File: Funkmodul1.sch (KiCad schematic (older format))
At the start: 48 parts, among them Q1 SSM3J334RLFTR-ND, Q2 AO3414, U1 MC74HC4538A, U2 MAX892, U3 ATMEGA128-16AU, Y1 Crystal_GND24

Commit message: Places µC of second module
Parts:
- Q1: symbol Q_PMOS_DGS -> Q_PMOS_SGD
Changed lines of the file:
@@
 $EndComp
 $Comp
-L GND #PWR11
+L GND #PWR01
 U 1 1 59FF9D54
 P 3200 1650
-F 0 "#PWR11" H 3200 1400 50  0001 C CNN
+F 0 "#PWR01" H 3200 1400 50  0001 C CNN
 F 1 "GND" H 3200 1500 50  0000 C CNN
 F 2 "" H 3200 1650 50  0001 C CNN
@@
 $EndComp
 $Comp
-L GND #PWR7
+L GND #PWR02
 U 1 1 59B7E738
 P 2250 1350
-F 0 "#PWR7" H 2250 1100 50  0001 C CNN
+F 0 "#PWR02" H 2250 1100 50  0001 C CNN
 F 1 "GND" H 2250 1200 50  0000 C CNN
 F 2 "" H 2250 1350 50  0001 C CNN
@@
 VCC
 $Comp
-L GND #PWR13
+L GND #PWR03
 U 1 1 59B80D24
 P 3750 2450
-F 0 "#PWR13" H 3750 2200 50  0001 C CNN
+F 0 "#PWR03" H 3750 2200 50  0001 C CNN
 F 1 "GND" H 3750 2300 50  0000 C CNN
 F 2 "" H 3750 2450 50  0001 C CNN
@@
 $EndComp
 $Comp
-L GND #PWR14
+L GND #PWR04
 U 1 1 59B80D8A
 P 3750 2850
-F 0 "#PWR14" H 3750 2600 50  0001 C CNN
+F 0 "#PWR04" H 3750 2600 50  0001 C CNN
 F 1 "GND" H 3750 2700 50  0000 C CNN
 F 2 "" H 3750 2850 50  0001 C CNN
@@
 $EndComp
 $Comp
-L GND #PWR17
+L GND #PWR05
 U 1 1 59B80E1B
 P 4300 3350
-F 0 "#PWR17" H 4300 3100 50  0001 C CNN
+F 0 "#PWR05" H 4300 3100 50  0001 C CNN
 F 1 "GND" H 4300 3200 50  0000 C CNN
 F 2 "" H 4300 3350 50  0001 C CNN
@@
 $EndComp
 $Comp
-L GND #PWR18
+L GND #PWR06
 U 1 1 59FF9D5A
 P 4550 2350
-F 0 "#PWR18" H 4550 2100 50  0001 C CNN
+F 0 "#PWR06" H 4550 2100 50  0001 C CNN
 F 1 "GND" H 4550 2200 50  0000 C CNN
 F 2 "" H 4550 2350 50  0001 C CNN
@@
 $EndComp
 $Comp
-L GND #PWR19
+L GND #PWR07
 U 1 1 59FF9D5B
 P 5000 2350
-F 0 "#PWR19" H 5000 2100 50  0001 C CNN
+F 0 "#PWR07" H 5000 2100 50  0001 C CNN
 F 1 "GND" H 5000 2200 50  0000 C CNN
 F 2 "" H 5000 2350 50  0001 C CNN
@@
 $EndComp
 $Comp
-L GND #PWR24
+L GND #PWR08
 U 1 1 59FF9D5C
 P 7000 1100
-F 0 "#PWR24" H 7000 850 50  0001 C CNN
+F 0 "#PWR08" H 7000 850 50  0001 C CNN
 F 1 "GND" H 7000 950 50  0000 C CNN
 F 2 "" H 7000 1100 50  0001 C CNN
@@
 $EndComp
 $Comp
-L GND #PWR21
+L GND #PWR09
 U 1 1 59FF9D5D
 P 6500 1150
-F 0 "#PWR21" H 6500 900 50  0001 C CNN
+F 0 "#PWR09" H 6500 900 50  0001 C CNN
 F 1 "GND" H 6500 1000 50  0000 C CNN
 F 2 "" H 6500 1150 50  0001 C CNN
@@
 $EndComp
 $Comp
-L GND #PWR20
+L GND #PWR010
 U 1 1 59FF9D5E
 P 6200 1150
-F 0 "#PWR20" H 6200 900 50  0001 C CNN
+F 0 "#PWR010" H 6200 900 50  0001 C CNN
 F 1 "GND" H 6200 1000 50  0000 C CNN
 F 2 "" H 6200 1150 50  0001 C CNN
@@
 $EndComp
 $Comp
-L GND #PWR22
+L GND #PWR011
 U 1 1 59B847A7
 P 6600 5700
-F 0 "#PWR22" H 6600 5450 50  0001 C CNN
+F 0 "#PWR011" H 6600 5450 50  0001 C CNN
 F 1 "GND" H 6600 5550 50  0000 C CNN
 F 2 "" H 6600 5700 50  0001 C CNN
@@
 $EndComp
 $Comp
-L GND #PWR23
+L GND #PWR012
 U 1 1 59B8480D
 P 6700 5700
-F 0 "#PWR23" H 6700 5450 50  0001 C CNN
+F 0 "#PWR012" H 6700 5450 50  0001 C CNN
 F 1 "GND" H 6700 5550 50  0000 C CNN
 F 2 "" H 6700 5700 50  0001 C CNN
@@
 $EndComp
 $Comp
-L GND #PWR25
+L GND #PWR013
 U 1 1 59B84873
 P 7000 5700
-F 0 "#PWR25" H 7000 5450 50  0001 C CNN
+F 0 "#PWR013" H 7000 5450 50  0001 C CNN
 F 1 "GND" H 7000 5550 50  0000 C CNN
 F 2 "" H 7000 5700 50  0001 C CNN
@@
 $EndComp
 $Comp
-L GND #PWR5
+L GND #PWR014
 U 1 1 59B8BFBA
 P 1650 2750
-F 0 "#PWR5" H 1650 2500 50  0001 C CNN
+F 0 "#PWR014" H 1650 2500 50  0001 C CNN
 F 1 "GND" H 1650 2600 50  0000 C CNN
 F 2 "" H 1650 2750 50  0001 C CNN
@@
 $EndComp
 $Comp
-L GND #PWR12
+L GND #PWR015
 U 1 1 59B8D4AD
 P 3600 750
-F 0 "#PWR12" H 3600 500 50  0001 C CNN
+F 0 "#PWR015" H 3600 500 50  0001 C CNN
 F 1 "GND" H 3600 600 50  0000 C CNN
 F 2 "" H 3600 750 50  0001 C CNN
@@
 $EndComp
 $Comp
-L GND #PWR6
+L GND #PWR016
 U 1 1 59FF9D6A
 P 1750 750
-F 0 "#PWR6" H 1750 500 50  0001 C CNN
+F 0 "#PWR016" H 1750 500 50  0001 C CNN
 F 1 "GND" H 1750 600 50  0000 C CNN
 F 2 "" H 1750 750 50  0001 C CNN
@@
 $EndComp
 $Comp
-L GND #PWR8
+L GND #PWR017
 U 1 1 59FF9D6F
 P 2650 4050
-F 0 "#PWR8" H 2650 3800 50  0001 C CNN
+F 0 "#PWR017" H 2650 3800 50  0001 C CNN
 F 1 "GND" H 2650 3900 50  0000 C CNN
 F 2 "" H 2650 4050 50  0001 C CNN
@@
 $EndComp
 $Comp
-L GND #PWR1
+L GND #PWR018
 U 1 1 59FF9D78
 P 600 1500
-F 0 "#PWR1" H 600 1250 50  0001 C CNN
+F 0 "#PWR018" H 600 1250 50  0001 C CNN
 F 1 "GND" H 600 1350 50  0000 C CNN
 F 2 "" H 600 1500 50  0001 C CNN
@@
 $EndComp
 $Comp
-L GND #PWR2
+L GND #PWR019
 U 1 1 59C31F10
 P 800 4850
-F 0 "#PWR2" H 800 4600 50  0001 C CNN
+F 0 "#PWR019" H 800 4600 50  0001 C CNN
 F 1 "GND" H 800 4700 50  0000 C CNN
 F 2 "" H 800 4850 50  0001 C CNN
@@
 $EndComp
 $Comp
-L GND #PWR10
+L GND #PWR020
 U 1 1 59C39B79
 P 2950 3100
-F 0 "#PWR10" H 2950 2850 50  0001 C CNN
+F 0 "#PWR020" H 2950 2850 50  0001 C CNN
 F 1 "GND" H 2950 2950 50  0000 C CNN
 F 2 "" H 2950 3100 50  0001 C CNN
@@
 $EndComp
 $Comp
-L GND #PWR3
+L GND #PWR021
 U 1 1 59C3C15C
 P 1350 3400
-F 0 "#PWR3" H 1350 3150 50  0001 C CNN
+F 0 "#PWR021" H 1350 3150 50  0001 C CNN
 F 1 "GND" H 1350 3250 50  0000 C CNN
 F 2 "" H 1350 3400 50  0001 C CNN
@@
 $EndComp
 $Comp
-L GND #PWR9
+L GND #PWR022
 U 1 1 59C3F3E3
 P 2700 5750
-F 0 "#PWR9" H 2700 5500 50  0001 C CNN
+F 0 "#PWR022" H 2700 5500 50  0001 C CNN
 F 1 "GND" H 2700 5600 50  0000 C CNN
 F 2 "" H 2700 5750 50  0001 C CNN
@@
 $EndComp
 $Comp
-L GND #PWR15
+L GND #PWR023
 U 1 1 59C3FC57
 P 3750 5550
-F 0 "#PWR15" H 3750 5300 50  0001 C CNN
+F 0 "#PWR023" H 3750 5300 50  0001 C CNN
 F 1 "GND" H 3750 5400 50  0000 C CNN
 F 2 "" H 3750 5550 50  0001 C CNN
@@
 $EndComp
 $Comp
-L GND #PWR16
+L GND #PWR024
 U 1 1 59C4457A
 P 3950 5500
-F 0 "#PWR16" H 3950 5250 50  0001 C CNN
+F 0 "#PWR024" H 3950 5250 50  0001 C CNN
 F 1 "GND" H 3950 5350 50  0000 C CNN
 F 2 "" H 3950 5500 50  0001 C CNN
@@
 VCC
 $Comp
-L GND #PWR26
+L GND #PWR025
 U 1 1 59D3B876
 P 9100 1450
-F 0 "#PWR26" H 9100 1200 50  0001 C CNN
+F 0 "#PWR025" H 9100 1200 50  0001 C CNN
 F 1 "GND" H 9100 1300 50  0000 C CNN
 F 2 "" H 9100 1450 50  0001 C CNN
@@
 $EndComp
 $Comp
-L GND #PWR4
+L GND #PWR026
 U 1 1 59FF9DAA
 P 1600 2400
-F 0 "#PWR4" H 1600 2150 50  0001 C CNN
+F 0 "#PWR026" H 1600 2150 50  0001 C CNN
 F 1 "GND" H 1600 2250 50  0000 C CNN
 F 2 "" H 1600 2400 50  0001 C CNN
@@
 3.3V
 $Comp
-L Q_PMOS_DGS Q1
+L Q_PMOS_SGD Q1
 U 1 1 59FF9DB0
 P 1400 1500

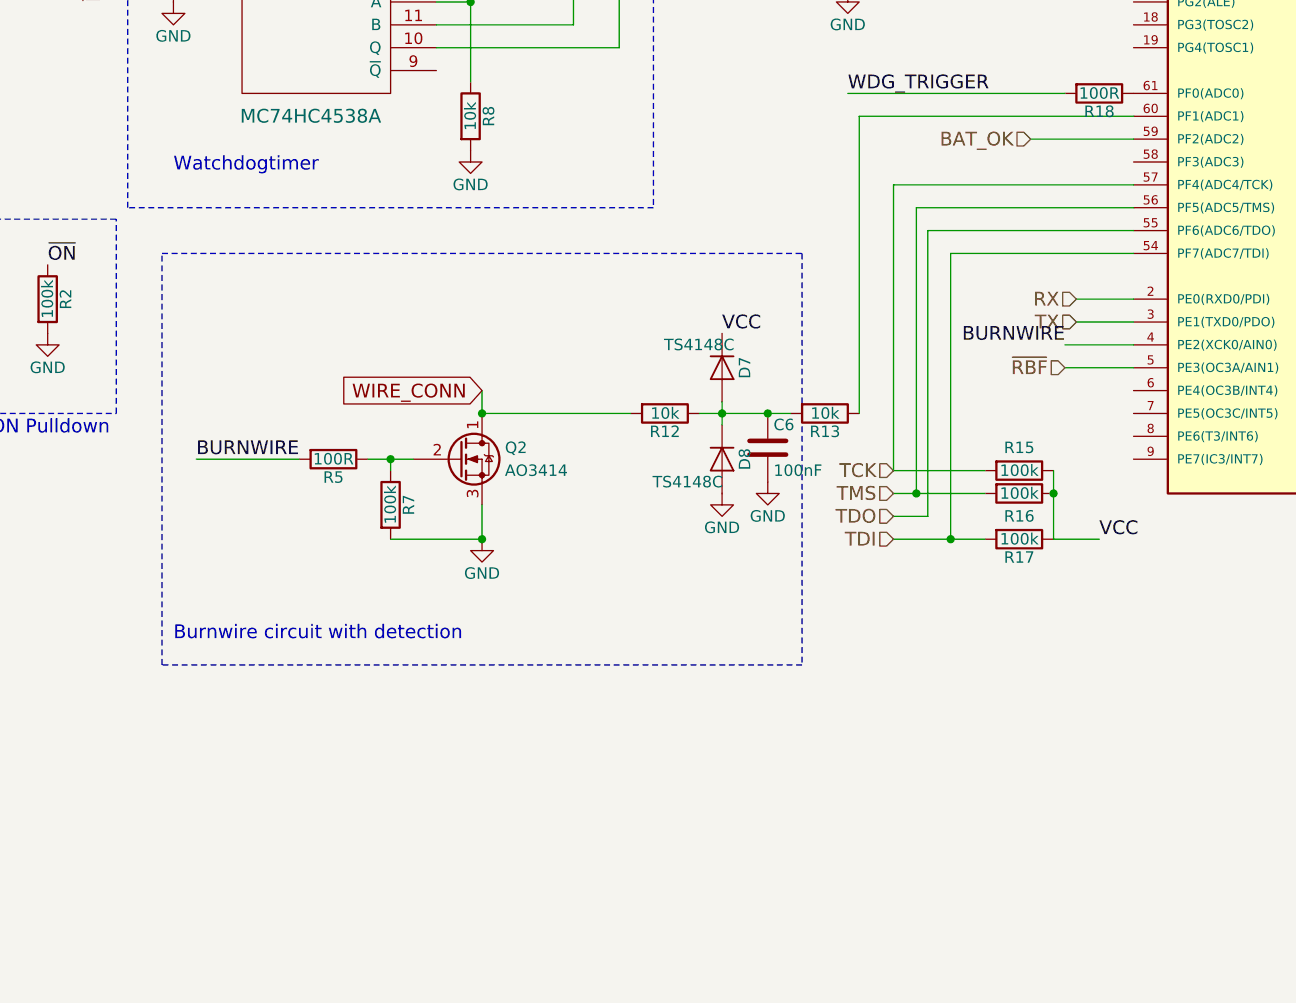
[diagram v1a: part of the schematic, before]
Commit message: Places all Components of second module
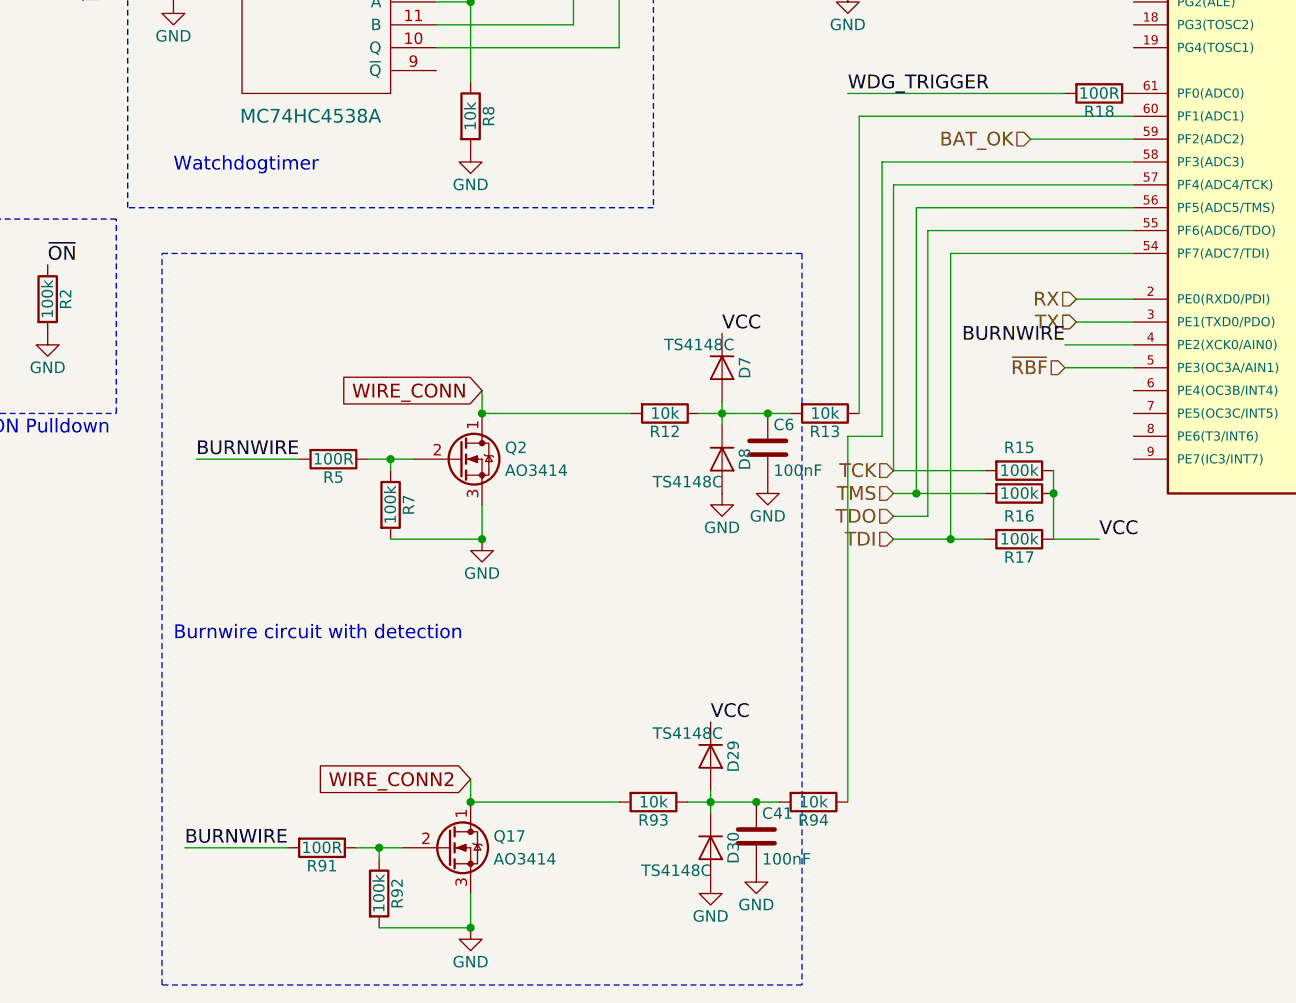
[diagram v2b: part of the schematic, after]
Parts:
- added C41: 100nF, Capacitors_SMD:C_0603_HandSoldering, symbol C
- added D29, D30: TS4148C, Diodes_SMD:D_0603, symbol D
- added Q17: AO3414, TO_SOT_Packages_SMD:SOT-23, symbol Q_NMOS_DGS
- added R91: 100R, Resistors_SMD:R_0603_HandSoldering, symbol R
- added R92: 100k, Resistors_SMD:R_0603_HandSoldering, symbol R
- added R93, R94: 10k, Resistors_SMD:R_0603_HandSoldering, symbol R
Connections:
- net BURNWIRE: now also R91.2
- net GND: now also C41.2, D30.2 (A), Q17.3 (S), R92.2
- net VCC: now also D29.1 (K)
- net at U3.58 (PF3(ADC3)): now also R94.1
- new net: Q17.2 (G), R91.1, R92.1
- new net: C41.1, D29.2 (A), D30.1 (K), R93.1, R94.2
- new net WIRE_CONN2: Q17.1 (D), R93.2

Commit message: Adds second burnwire fets
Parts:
- removed R15, R16, R17: 100k, Resistors_SMD:R_0603_HandSoldering, symbol R
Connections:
- net BURNWIRE: no longer R91.2
- net BURNWIRE2: now reaches U3.6 (PE4(OC3B/INT4))
- net BURNWIRE2: now also R91.2
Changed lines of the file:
@@
 $EndComp
 $Comp
-L GND #PWR12
+L GND #PWR01
 U 1 1 59FF9D54
 P 3200 1650
-F 0 "#PWR12" H 3200 1400 50  0001 C CNN
+F 0 "#PWR01" H 3200 1400 50  0001 C CNN
 F 1 "GND" H 3200 1500 50  0000 C CNN
 F 2 "" H 3200 1650 50  0001 C CNN
@@
 $EndComp
 $Comp
-L GND #PWR7
+L GND #PWR02
 U 1 1 59B7E738
 P 2250 1350
-F 0 "#PWR7" H 2250 1100 50  0001 C CNN
+F 0 "#PWR02" H 2250 1100 50  0001 C CNN
 F 1 "GND" H 2250 1200 50  0000 C CNN
 F 2 "" H 2250 1350 50  0001 C CNN
@@
 VCC
 $Comp
-L GND #PWR15
+L GND #PWR03
 U 1 1 59B80D24
 P 3750 2450
-F 0 "#PWR15" H 3750 2200 50  0001 C CNN
+F 0 "#PWR03" H 3750 2200 50  0001 C CNN
 F 1 "GND" H 3750 2300 50  0000 C CNN
 F 2 "" H 3750 2450 50  0001 C CNN
@@
 $EndComp
 $Comp
-L GND #PWR16
+L GND #PWR04
 U 1 1 59B80D8A
 P 3750 2850
-F 0 "#PWR16" H 3750 2600 50  0001 C CNN
+F 0 "#PWR04" H 3750 2600 50  0001 C CNN
 F 1 "GND" H 3750 2700 50  0000 C CNN
 F 2 "" H 3750 2850 50  0001 C CNN
@@
 $EndComp
 $Comp
-L GND #PWR20
+L GND #PWR05
 U 1 1 59B80E1B
 P 4300 3350
-F 0 "#PWR20" H 4300 3100 50  0001 C CNN
+F 0 "#PWR05" H 4300 3100 50  0001 C CNN
 F 1 "GND" H 4300 3200 50  0000 C CNN
 F 2 "" H 4300 3350 50  0001 C CNN
@@
 $EndComp
 $Comp
-L GND #PWR21
+L GND #PWR06
 U 1 1 59FF9D5A
 P 4550 2350
-F 0 "#PWR21" H 4550 2100 50  0001 C CNN
+F 0 "#PWR06" H 4550 2100 50  0001 C CNN
 F 1 "GND" H 4550 2200 50  0000 C CNN
 F 2 "" H 4550 2350 50  0001 C CNN
@@
 $EndComp
 $Comp
-L GND #PWR22
+L GND #PWR07
 U 1 1 59FF9D5B
 P 5000 2350
-F 0 "#PWR22" H 5000 2100 50  0001 C CNN
+F 0 "#PWR07" H 5000 2100 50  0001 C CNN
 F 1 "GND" H 5000 2200 50  0000 C CNN
 F 2 "" H 5000 2350 50  0001 C CNN
@@
 $EndComp
 $Comp
-L GND #PWR27
+L GND #PWR08
 U 1 1 59FF9D5C
 P 7000 1100
-F 0 "#PWR27" H 7000 850 50  0001 C CNN
+F 0 "#PWR08" H 7000 850 50  0001 C CNN
 F 1 "GND" H 7000 950 50  0000 C CNN
 F 2 "" H 7000 1100 50  0001 C CNN
@@
 $EndComp
 $Comp
-L GND #PWR24
+L GND #PWR09
 U 1 1 59FF9D5D
 P 6500 1150
-F 0 "#PWR24" H 6500 900 50  0001 C CNN
+F 0 "#PWR09" H 6500 900 50  0001 C CNN
 F 1 "GND" H 6500 1000 50  0000 C CNN
 F 2 "" H 6500 1150 50  0001 C CNN
@@
 $EndComp
 $Comp
-L GND #PWR23
+L GND #PWR010
 U 1 1 59FF9D5E
 P 6200 1150
-F 0 "#PWR23" H 6200 900 50  0001 C CNN
+F 0 "#PWR010" H 6200 900 50  0001 C CNN
 F 1 "GND" H 6200 1000 50  0000 C CNN
 F 2 "" H 6200 1150 50  0001 C CNN
@@
 $EndComp
 $Comp
-L GND #PWR25
+L GND #PWR011
 U 1 1 59B847A7
 P 6600 5700
-F 0 "#PWR25" H 6600 5450 50  0001 C CNN
+F 0 "#PWR011" H 6600 5450 50  0001 C CNN
 F 1 "GND" H 6600 5550 50  0000 C CNN
 F 2 "" H 6600 5700 50  0001 C CNN
@@
 $EndComp
 $Comp
-L GND #PWR26
+L GND #PWR012
 U 1 1 59B8480D
 P 6700 5700
-F 0 "#PWR26" H 6700 5450 50  0001 C CNN
+F 0 "#PWR012" H 6700 5450 50  0001 C CNN
 F 1 "GND" H 6700 5550 50  0000 C CNN
 F 2 "" H 6700 5700 50  0001 C CNN
@@
 $EndComp
 $Comp
-L GND #PWR28
+L GND #PWR013
 U 1 1 59B84873
 P 7000 5700
-F 0 "#PWR28" H 7000 5450 50  0001 C CNN
+F 0 "#PWR013" H 7000 5450 50  0001 C CNN
 F 1 "GND" H 7000 5550 50  0000 C CNN
 F 2 "" H 7000 5700 50  0001 C CNN
@@
 $EndComp
 $Comp
-L GND #PWR5
+L GND #PWR014
 U 1 1 59B8BFBA
 P 1650 2750
-F 0 "#PWR5" H 1650 2500 50  0001 C CNN
+F 0 "#PWR014" H 1650 2500 50  0001 C CNN
 F 1 "GND" H 1650 2600 50  0000 C CNN
 F 2 "" H 1650 2750 50  0001 C CNN
@@
 $EndComp
 $Comp
-L GND #PWR13
+L GND #PWR015
 U 1 1 59B8D4AD
 P 3600 750
-F 0 "#PWR13" H 3600 500 50  0001 C CNN
+F 0 "#PWR015" H 3600 500 50  0001 C CNN
 F 1 "GND" H 3600 600 50  0000 C CNN
 F 2 "" H 3600 750 50  0001 C CNN
@@
 $EndComp
 $Comp
-L GND #PWR6
+L GND #PWR016
 U 1 1 59FF9D6A
 P 1750 750
-F 0 "#PWR6" H 1750 500 50  0001 C CNN
+F 0 "#PWR016" H 1750 500 50  0001 C CNN
 F 1 "GND" H 1750 600 50  0000 C CNN
 F 2 "" H 1750 750 50  0001 C CNN
@@
 $EndComp
 $Comp
-L GND #PWR8
+L GND #PWR017
 U 1 1 59FF9D6F
 P 2650 4050
-F 0 "#PWR8" H 2650 3800 50  0001 C CNN
+F 0 "#PWR017" H 2650 3800 50  0001 C CNN
 F 1 "GND" H 2650 3900 50  0000 C CNN
 F 2 "" H 2650 4050 50  0001 C CNN
@@
 $EndComp
 $Comp
-L GND #PWR1
+L GND #PWR018
 U 1 1 59FF9D78
 P 600 1500
-F 0 "#PWR1" H 600 1250 50  0001 C CNN
+F 0 "#PWR018" H 600 1250 50  0001 C CNN
 F 1 "GND" H 600 1350 50  0000 C CNN
 F 2 "" H 600 1500 50  0001 C CNN
@@
 $EndComp
 $Comp
-L GND #PWR2
+L GND #PWR019
 U 1 1 59C31F10
 P 800 4850
-F 0 "#PWR2" H 800 4600 50  0001 C CNN
+F 0 "#PWR019" H 800 4600 50  0001 C CNN
 F 1 "GND" H 800 4700 50  0000 C CNN
 F 2 "" H 800 4850 50  0001 C CNN
@@
 $EndComp
 $Comp
-L GND #PWR11
+L GND #PWR020
 U 1 1 59C39B79
 P 2950 3100
-F 0 "#PWR11" H 2950 2850 50  0001 C CNN
+F 0 "#PWR020" H 2950 2850 50  0001 C CNN
 F 1 "GND" H 2950 2950 50  0000 C CNN
 F 2 "" H 2950 3100 50  0001 C CNN
@@
 $EndComp
 $Comp
-L GND #PWR3
+L GND #PWR021
 U 1 1 59C3C15C
 P 1350 3400
-F 0 "#PWR3" H 1350 3150 50  0001 C CNN
+F 0 "#PWR021" H 1350 3150 50  0001 C CNN
 F 1 "GND" H 1350 3250 50  0000 C CNN
 F 2 "" H 1350 3400 50  0001 C CNN
@@
 $EndComp
 $Comp
-L GND #PWR10
+L GND #PWR022
 U 1 1 59C3F3E3
 P 2700 5750
-F 0 "#PWR10" H 2700 5500 50  0001 C CNN
+F 0 "#PWR022" H 2700 5500 50  0001 C CNN
 F 1 "GND" H 2700 5600 50  0000 C CNN
 F 2 "" H 2700 5750 50  0001 C CNN
@@
 $EndComp
 $Comp
-L GND #PWR17
+L GND #PWR023
 U 1 1 59C3FC57
 P 3750 5550
-F 0 "#PWR17" H 3750 5300 50  0001 C CNN
+F 0 "#PWR023" H 3750 5300 50  0001 C CNN
 F 1 "GND" H 3750 5400 50  0000 C CNN
 F 2 "" H 3750 5550 50  0001 C CNN
@@
 $EndComp
 $Comp
-L GND #PWR19
+L GND #PWR024
 U 1 1 59C4457A
 P 3950 5500
-F 0 "#PWR19" H 3950 5250 50  0001 C CNN
+F 0 "#PWR024" H 3950 5250 50  0001 C CNN
 F 1 "GND" H 3950 5350 50  0000 C CNN
 F 2 "" H 3950 5500 50  0001 C CNN
@@
 VCC
 $Comp
-L GND #PWR29
+L GND #PWR025
 U 1 1 59D3B876
 P 9100 1450
-F 0 "#PWR29" H 9100 1200 50  0001 C CNN
+F 0 "#PWR025" H 9100 1200 50  0001 C CNN
 F 1 "GND" H 9100 1300 50  0000 C CNN
 F 2 "" H 9100 1450 50  0001 C CNN
@@
 Text HLabel 4500 5750 0    60   Input ~ 0
 TDI
-$Comp
-L R R15
-U 1 1 59FF9DA6
-P 5050 5450
-F 0 "R15" V 4950 5450 50  0000 C CNN
-F 1 "100k" V 5050 5450 50  0000 C CNN
-F 2 "Resistors_SMD:R_0603_HandSoldering" V 4980 5450 50  0001 C CNN
-F 3 "" H 5050 5450 50  0001 C CNN
-	1    5050 5450
-	0    1    1    0
-$EndComp
-$Comp
-L R R16
-U 1 1 59FF9DA7
-P 5050 5550
-F 0 "R16" V 5150 5550 50  0000 C CNN
-F 1 "100k" V 5050 5550 50  0000 C CNN
-F 2 "Resistors_SMD:R_0603_HandSoldering" V 4980 5550 50  0001 C CNN
-F 3 "" H 5050 5550 50  0001 C CNN
-	1    5050 5550
-	0    1    1    0
-$EndComp
-$Comp
-L R R17
-U 1 1 59FF9DA8
-P 5050 5750
-F 0 "R17" V 5130 5750 50  0000 C CNN
-F 1 "100k" V 5050 5750 50  0000 C CNN
-F 2 "Resistors_SMD:R_0603_HandSoldering" V 4980 5750 50  0001 C CNN
-F 3 "" H 5050 5750 50  0001 C CNN
-	1    5050 5750
-	0    1    1    0
-$EndComp
-Text Label 5400 5750 0    60   ~ 0
-VCC
 Text HLabel 5100 4000 0    60   Input ~ 0
 BAT_OK
@@
 $EndComp
 $Comp
-L GND #PWR4
+L GND #PWR026
 U 1 1 59FF9DAA
 P 1600 2400
-F 0 "#PWR4" H 1600 2150 50  0001 C CNN
+F 0 "#PWR026" H 1600 2150 50  0001 C CNN
 F 1 "GND" H 1600 2250 50  0000 C CNN
 F 2 "" H 1600 2400 50  0001 C CNN
@@
 	4600 4300 4600 5550
 Wire Wire Line
-	4500 5550 4900 5550
-Wire Wire Line
 	5550 4400 4650 4400
 Wire Wire Line
@@
 Wire Wire Line
 	4750 4500 4750 5750
-Wire Wire Line
-	4500 5750 4900 5750
-Wire Wire Line
-	4500 5450 4900 5450
 Connection ~ 4600 5550
 Connection ~ 4750 5750
 Wire Wire Line
 	4650 5650 4500 5650
-Wire Wire Line
-	5200 5450 5200 5750
-Wire Wire Line
-	5200 5750 5400 5750
-Connection ~ 5200 5550
 Wire Wire Line
 	5100 4000 5550 4000
@@
 $EndComp
 $Comp
-L GND #PWR9
+L GND #PWR027
 U 1 1 5A075389
 P 2650 7450
-F 0 "#PWR9" H 2650 7200 50  0001 C CNN
+F 0 "#PWR027" H 2650 7200 50  0001 C CNN
 F 1 "GND" H 2650 7300 50  0000 C CNN
 F 2 "" H 2650 7450 50  0001 C CNN
@@
 $EndComp
 Text Label 1400 7100 0    60   ~ 0
-BURNWIRE
+BURNWIRE2
 Text GLabel 2650 6800 0    60   Input ~ 0
 WIRE_CONN2
@@
 $EndComp
 $Comp
-L GND #PWR14
+L GND #PWR028
 U 1 1 5A075397
 P 3700 7250
-F 0 "#PWR14" H 3700 7000 50  0001 C CNN
+F 0 "#PWR028" H 3700 7000 50  0001 C CNN
 F 1 "GND" H 3700 7100 50  0000 C CNN
 F 2 "" H 3700 7250 50  0001 C CNN
@@
 $EndComp
 $Comp
-L GND #PWR18
+L GND #PWR029
 U 1 1 5A0753B0
 P 3900 7200
-F 0 "#PWR18" H 3900 6950 50  0001 C CNN
+F 0 "#PWR029" H 3900 6950 50  0001 C CNN
 F 1 "GND" H 3900 7050 50  0000 C CNN
 F 2 "" H 3900 7200 50  0001 C CNN
@@
 Wire Wire Line
 	4450 4100 5550 4100
+Wire Wire Line
+	4600 5550 4500 5550
+Wire Wire Line
+	4750 5750 4500 5750
+Wire Wire Line
+	5550 5100 5250 5100
+Text Label 5250 5100 2    60   ~ 0
+BURNWIRE2
 $EndSCHEMATC

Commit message: Adds BOM and production files
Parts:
- added R15: 0R, Resistors_SMD:R_0805_HandSoldering, symbol R
- Y1: value Crystal_GND24 -> 407F39D007M3728; footprint Crystals:Crystal_SMD_3225-4pin_3.2x2.5mm_HandSoldering -> Crystals:Crystal_SMD_7050-4pin_7.0x5.0mm
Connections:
- net ~ON~: now also R6.1, U1.10 (Q), U1.5 (B), R15.1; no longer D6.1 (K)
- net RESET_3V3: now reaches U3.29 ((ICP1)PD4)
- new net: D6.1 (K), R15.2
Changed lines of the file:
@@
 Text Label 2000 1250 0    60   ~ 0
-~ON~
-Text Label 3000 2600 0    60   ~ 0
 ~ON~
 Text Label 3100 2300 0    60   ~ 0
@@
 P 3750 2650
 F 0 "Y1" H 3875 2850 50  0000 L CNN
-F 1 "Crystal_GND24" H 3875 2775 50  0000 L CNN
-F 2 "Crystals:Crystal_SMD_3225-4pin_3.2x2.5mm_HandSoldering" H 3750 2650 50  0001 C CNN
+F 1 "407F39D007M3728" H 3875 2775 50  0000 L CNN
+F 2 "Crystals:Crystal_SMD_7050-4pin_7.0x5.0mm" H 3750 2650 50  0001 C CNN
 F 3 "" H 3750 2650 50  0001 C CNN
 	1    3750 2650
@@
 Text Label 5250 5100 2    60   ~ 0
 BURNWIRE2
+Text HLabel 8150 5100 2    60   Input ~ 0
+RESET_3V3
+Text Label 3300 2600 0    60   ~ 0
+~ON~
+$Comp
+L R R15
+U 1 1 5A0FBAB8
+P 3150 2600
+F 0 "R15" V 3230 2600 50  0000 C CNN
+F 1 "0R" V 3150 2600 50  0000 C CNN
+F 2 "Resistors_SMD:R_0805_HandSoldering" V 3080 2600 50  0001 C CNN
+F 3 "" H 3150 2600 50  0001 C CNN
+	1    3150 2600
+	0    1    1    0
+$EndComp
 $EndSCHEMATC
